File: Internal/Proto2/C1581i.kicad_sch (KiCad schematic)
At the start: 73 parts, among them CN1 FLOPPY POWER, CN2 FLOPPY, CN5 LEDS, CN7 INTERNAL IEC, CN8 EXTERNAL POWER, J1 PIN34, J2 PIN2, J3 PIN2, J4 FPC, J5 ROM SELECT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

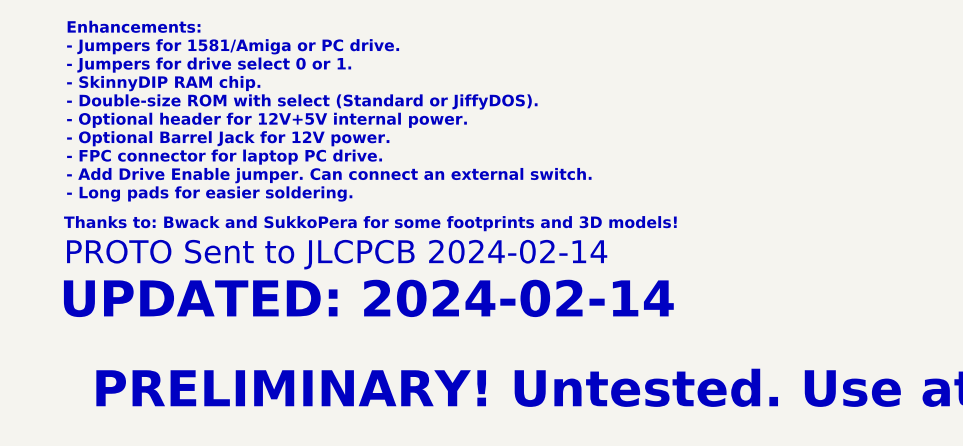
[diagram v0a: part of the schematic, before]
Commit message: Add EMI component values
Add missing EMI component values and generated new Interactive BOMs for both Enhanced and Internal Proto2 designs.
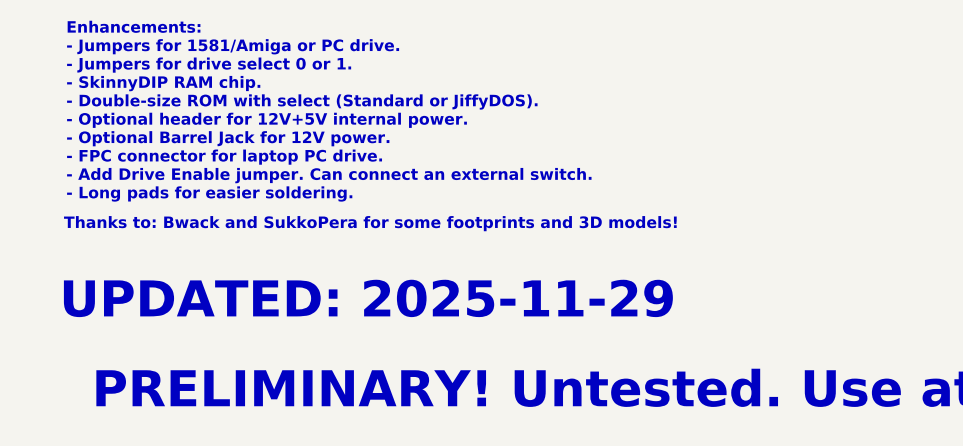
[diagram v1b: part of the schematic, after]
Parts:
- EM1, EM2, EM3, EM4: value EMI -> 100pf
- FB1, FB2, FB3, FB4, FB5, FB6: value R -> FB
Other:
- note added: "UPDATED: 2025-11-29"
- note removed: "PROTO Sent to JLCPCB 2024-02-14"
- note removed: "UPDATED: 2024-02-14"
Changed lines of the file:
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@@
 		(title "C1581i Disk Drive PCB")
 		(date "2025-09-16")
-		(rev "V1.1")
+		(rev "V2")
 		(company "Steve J. Gray")
 	)
@@
 		)
 	)
-	(text "UPDATED: 2024-02-14"
+	(text "UPDATED: 2025-11-29"
 		(exclude_from_sim no)
 		(at 13.208 284.226 0)
@@
 		)
 	)
-	(text "PROTO Sent to JLCPCB 2024-02-14"
-		(exclude_from_sim no)
-		(at 13.716 278.13 0)
-		(effects
-			(font
-				(size 2.54 2.54)
-			)
-			(justify left bottom)
-		)
-	)
 	(text "Reduced Wr\nSpare\nSelect 3\nIndex\nSelect0\nSelect1\nSelect2\nMotorEn\nDirection\nStep\nWriteData\nWriteGate\nTrack00\nWriteProt\nReadData\nSideSelect\nDiskChg\n"
 		(exclude_from_sim no)
@@
 			)
 		)
-		(property "Value" "R"
+		(property "Value" "FB"
 			(at 32.9946 60.0202 0)
 			(effects
@@
 			)
 		)
-		(property "Value" "EMI"
+		(property "Value" "100pf"
 			(at 377.0122 179.4002 0)
 			(effects
@@
 			)
 		)
-		(property "Value" "R"
+		(property "Value" "FB"
 			(at 101.6 181.864 0)
 			(effects
@@
 			)
 		)
-		(property "Value" "EMI"
+		(property "Value" "100pf"
 			(at 376.8344 148.3614 0)
 			(effects
@@
 			)
 		)
-		(property "Value" "R"
+		(property "Value" "FB"
 			(at 63.5 171.704 0)
 			(effects
@@
 			)
 		)
-		(property "Value" "EMI"
+		(property "Value" "100pf"
 			(at 376.2502 136.1186 0)
 			(effects
@@
 			)
 		)
-		(property "Value" "R"
+		(property "Value" "FB"
 			(at 53.34 162.306 0)
 			(effects
@@
 			)
 		)
-		(property "Value" "R"
+		(property "Value" "FB"
 			(at 104.14 171.704 0)
 			(effects
@@
 			)
 		)
-		(property "Value" "R"
+		(property "Value" "FB"
 			(at 32.9946 53.6702 0)
 			(effects
@@
 			)
 		)
-		(property "Value" "EMI"
+		(property "Value" "100pf"
 			(at 377.1392 163.6522 0)
 			(effects
